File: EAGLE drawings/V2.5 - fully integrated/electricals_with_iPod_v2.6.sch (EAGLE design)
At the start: 47 parts, among them IC1 ATMEGA32U2-TQFP, Y1 16MHz

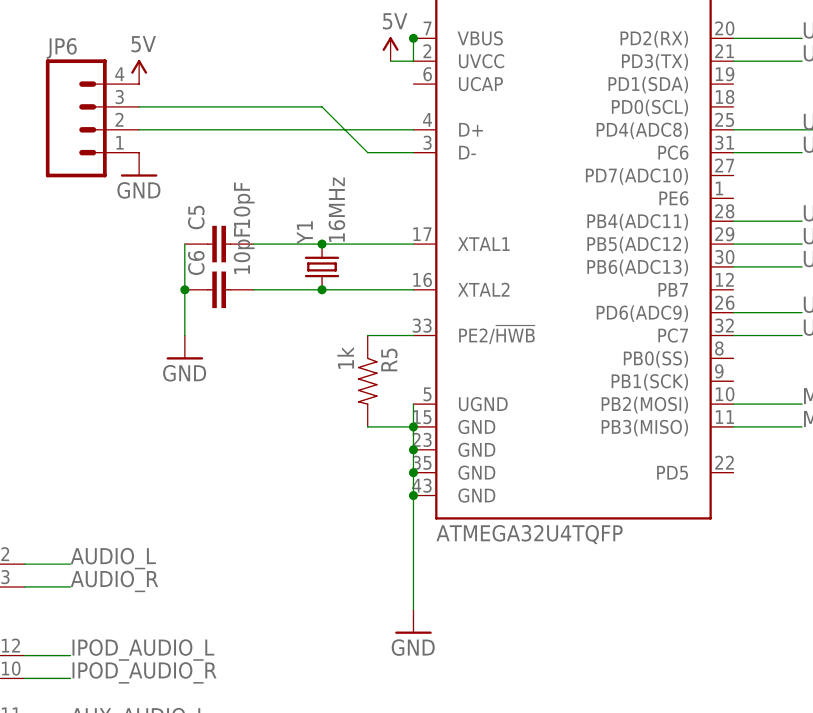
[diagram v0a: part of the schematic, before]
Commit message: Added v2.6 - smaller, 0603 passives, QFN mega*U4
Files edited with EAGLE 7.1.0
Split off v2.6
 - board about .25” shorter
 - 0603 passives
 - QFN package ATMega*U4
 - rearranged power supply
 - tweaked iPod connector board
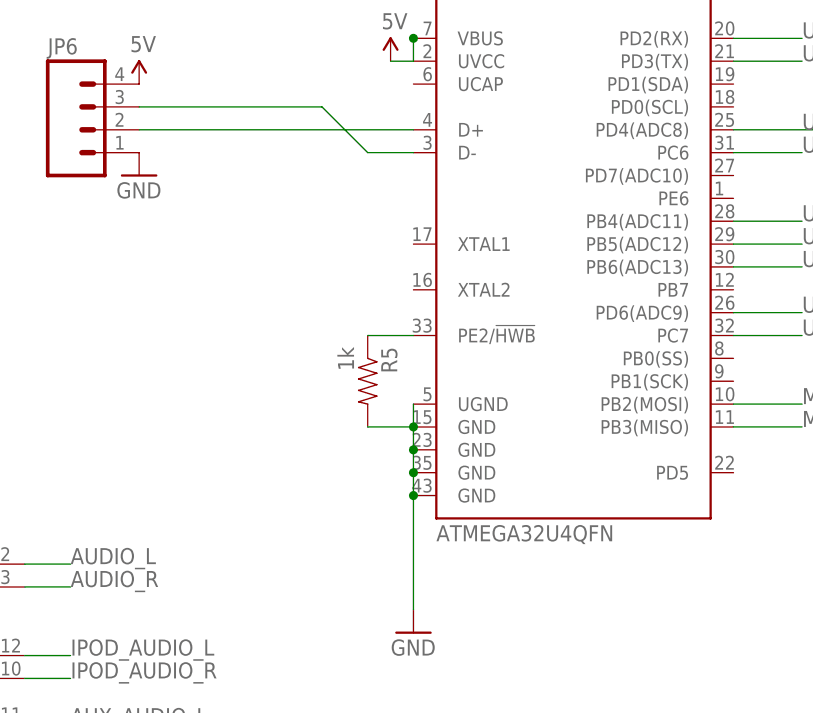
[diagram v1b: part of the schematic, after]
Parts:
- removed C5, C6: 10pF, SparkFun-Passives:CAP0805
- removed Y1: 16MHz, SparkFun-FreqCtrl:CRYSTAL5X3
- C1, C2, C3, C4, C7, C8, C9: device SparkFun-Passives:CAP0805 -> SparkFun-Passives:CAP0603-CAP
- R1, R2, R3, R4, R5, R6, R7: device SparkFun-Resistors:RESISTOR0805-RES -> SparkFun-Resistors:RESISTOR0603-RES
- U$8: value ATMEGA32U4TQFP -> ATMEGA32U4QFN; device SparkFun-DigitalIC:ATMEGA32U4TQFP -> SparkFun-DigitalIC:ATMEGA32U4QFN
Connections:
- removed net N$15: C5.2, U$8.XTAL1, Y1.2
- removed net N$28: C6.2, U$8.XTAL2, Y1.1
- net GND: no longer C5.1, C6.1

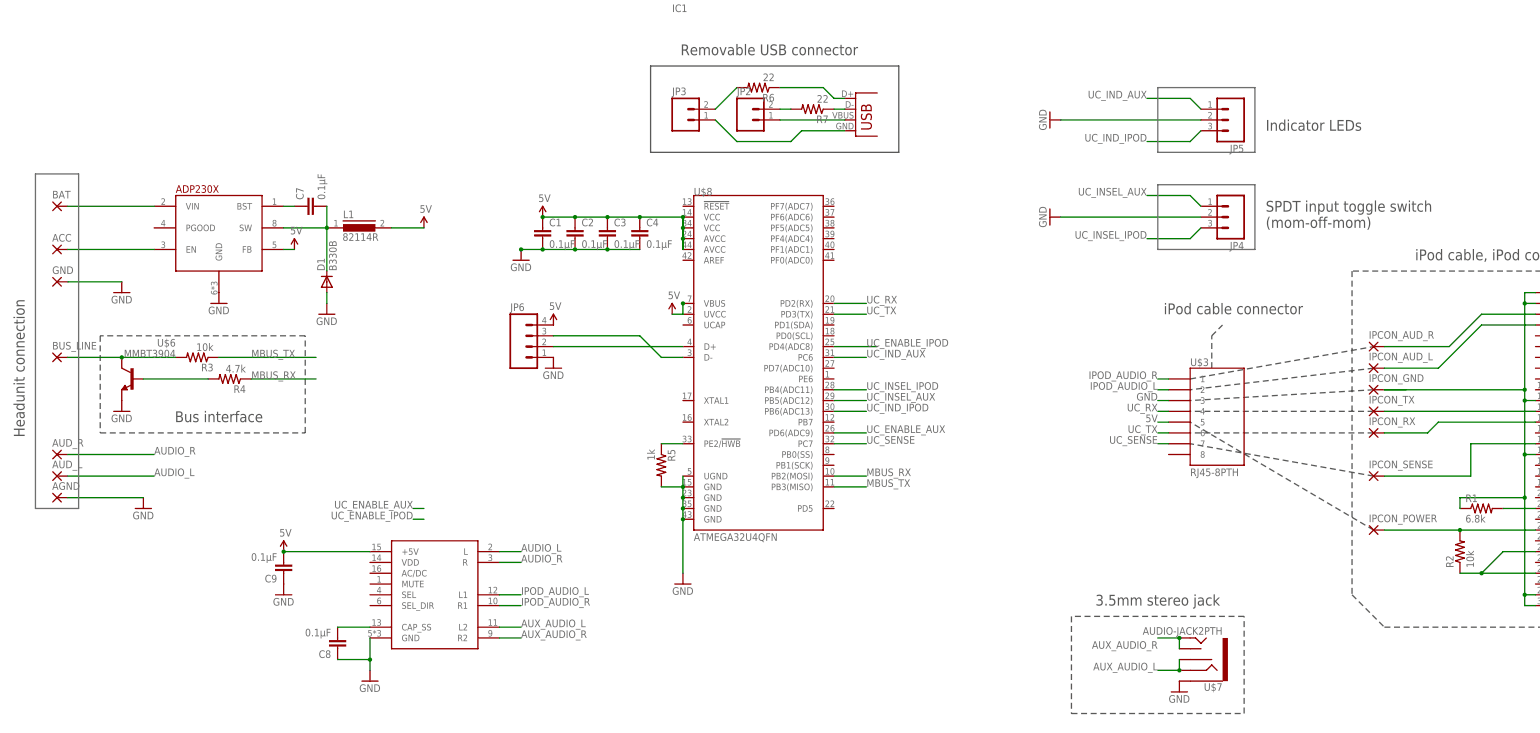
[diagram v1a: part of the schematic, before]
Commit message: iPod breakout split from v2.6, new single-input board
The iPod connector board was pulled from V2.6 to send to OSHPark

v2.6 is pending revisions down from the ATMega 16U4 to [8|16|32]U2. May
shrink more.

A new board is in the works that can fit on the back of the stereo
connector, providing only an auxiliary input. Uses an ATTiny.
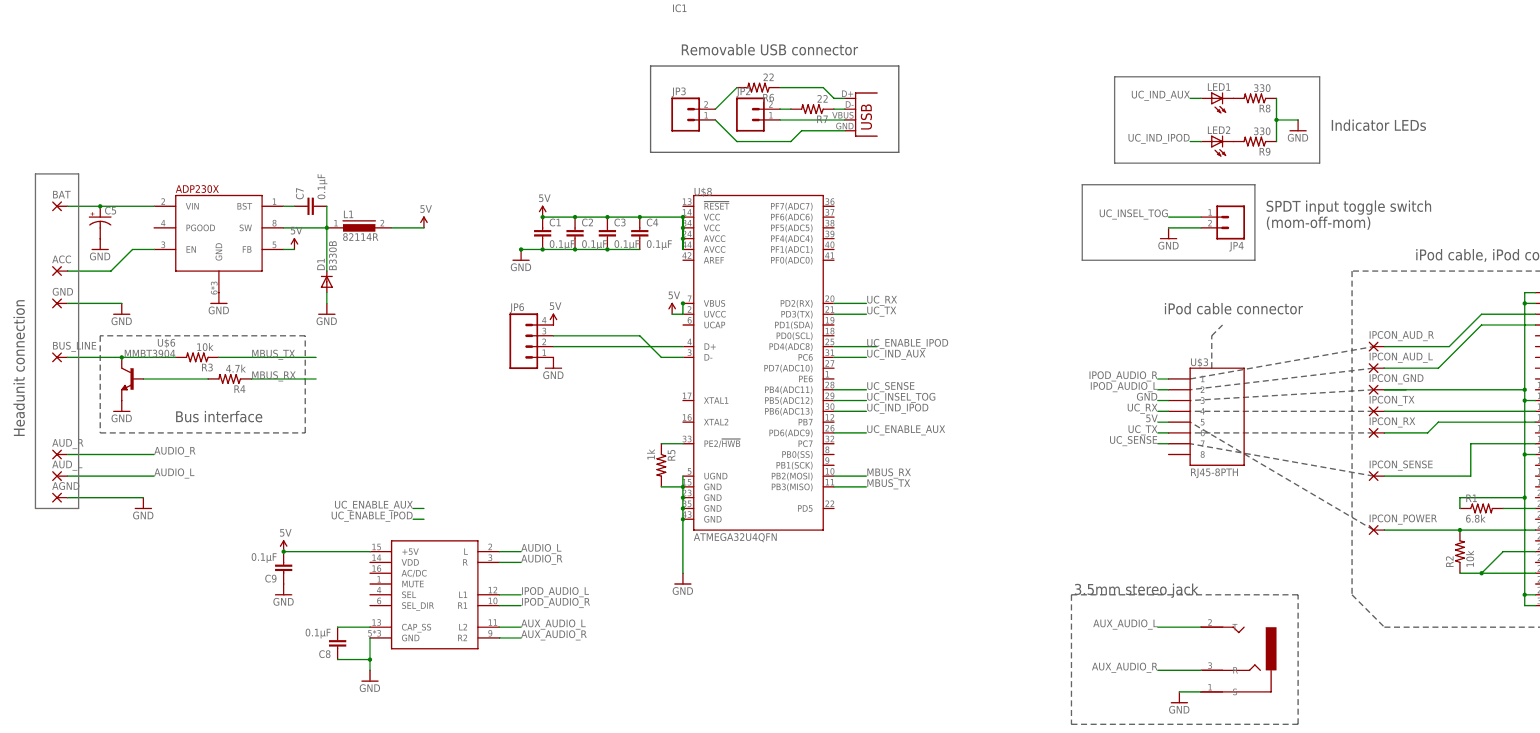
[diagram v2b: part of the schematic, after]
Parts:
- removed JP5: (no value), SparkFun-Connectors:M03LOCK
- added C5: (no value), SparkFun-Capacitors:CAP_POLPTH2
- added LED1, LED2: (no value), SparkFun-LED:LED0603
- added R8, R9: 330, SparkFun-Resistors:RESISTOR0603-RES
- JP4: device SparkFun-Connectors:M03LOCK -> SparkFun-Connectors:M02LOCK
- U$7: value AUDIO-JACK2PTH -> STEREO_JACK_SJ1-353XNG3NG; device SparkFun-Connectors:AUDIO-JACK2PTH -> personal:STEREO_JACK_SJ1-353XNG3NG
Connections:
- net UC_INSEL_AUX renamed UC_INSEL_TOG
- removed net UC_INSEL_IPOD: JP4.3, U$8.PB4(ADC11)
- new net N$15: LED1.C, R8.2
- new net N$16: LED2.C, R9.2
- net AUX_AUDIO_L: now also U$7.T; no longer U$7.RING, U$7.RSH
- net AUX_AUDIO_R: now also U$7.R; no longer U$7.TIP, U$7.TSH
- net GND: now also C5.-, R8.1, R9.1, U$7.S; no longer JP5.2, U$7.SLEEVE
- net N$2: now also C5.+
- net UC_IND_AUX: now also LED1.A; no longer JP5.1
- net UC_IND_IPOD: now also LED2.A; no longer JP5.3
- net UC_SENSE: now also U$8.PB4(ADC11); no longer U$8.PC7
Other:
- moved on the sheet: ACC, GND

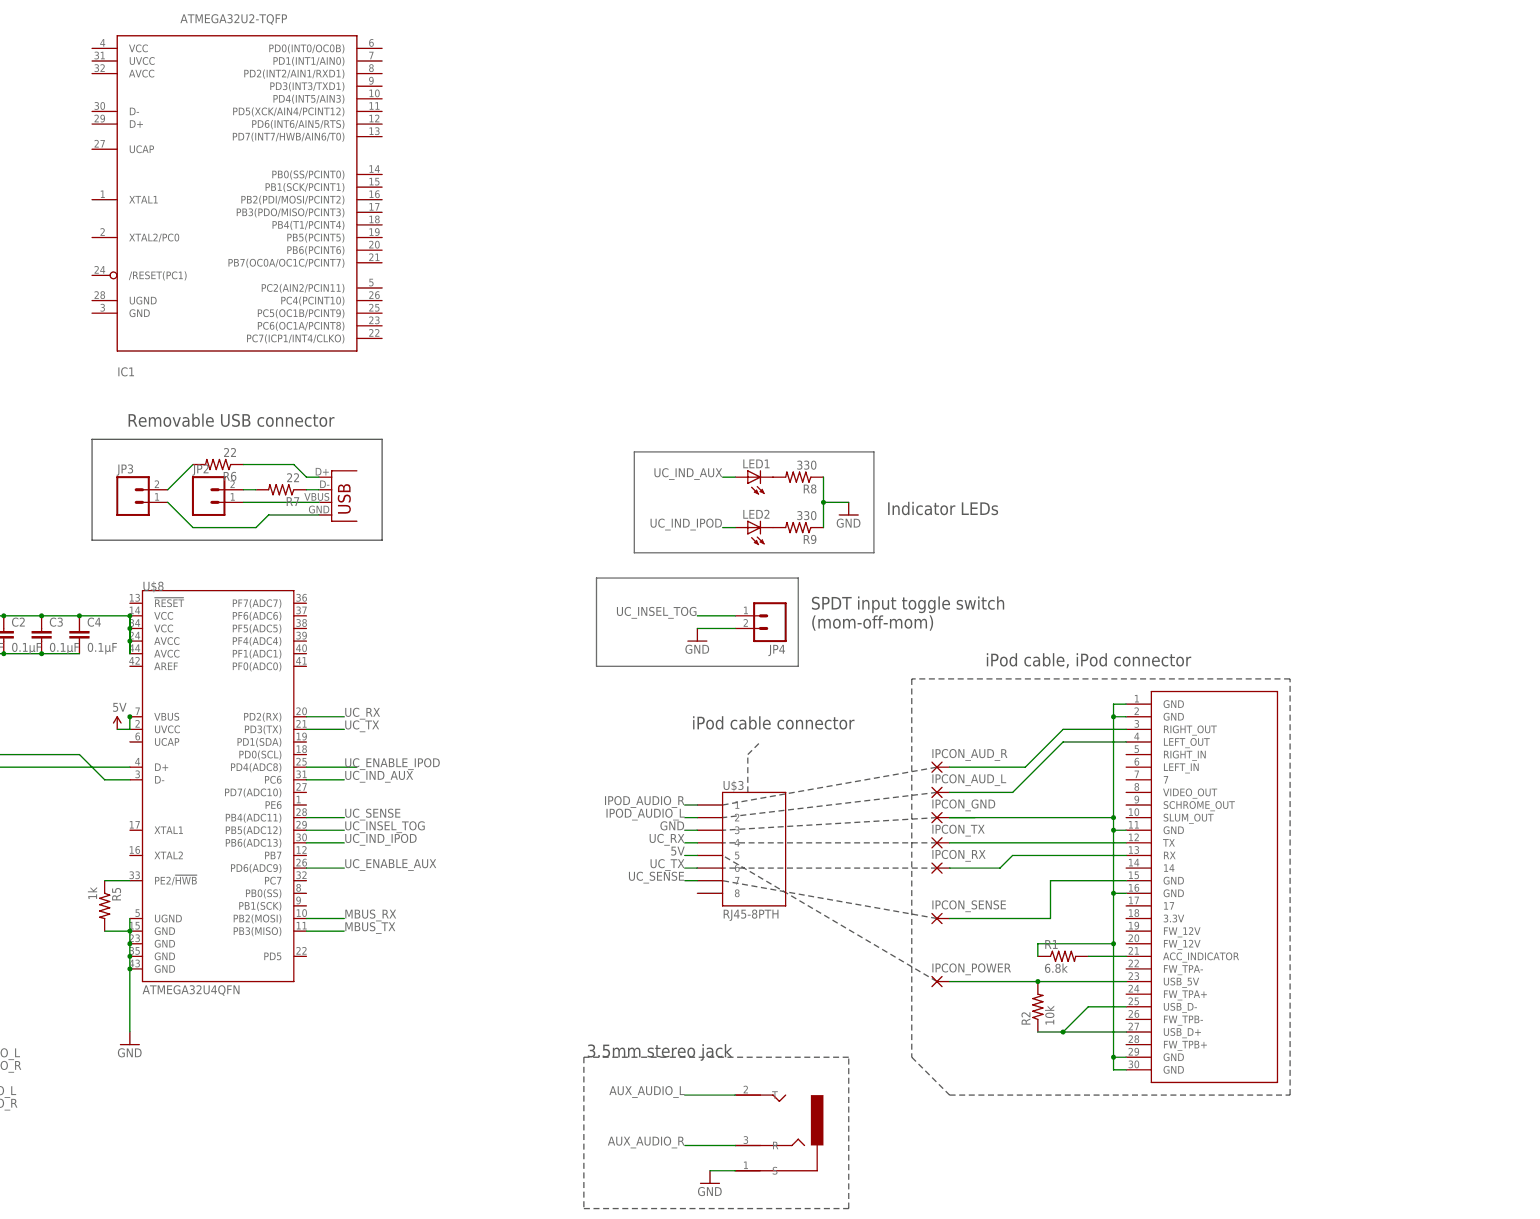
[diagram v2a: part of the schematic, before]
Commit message: Updated aux-only board, preparing to switch to 32/16/8U2
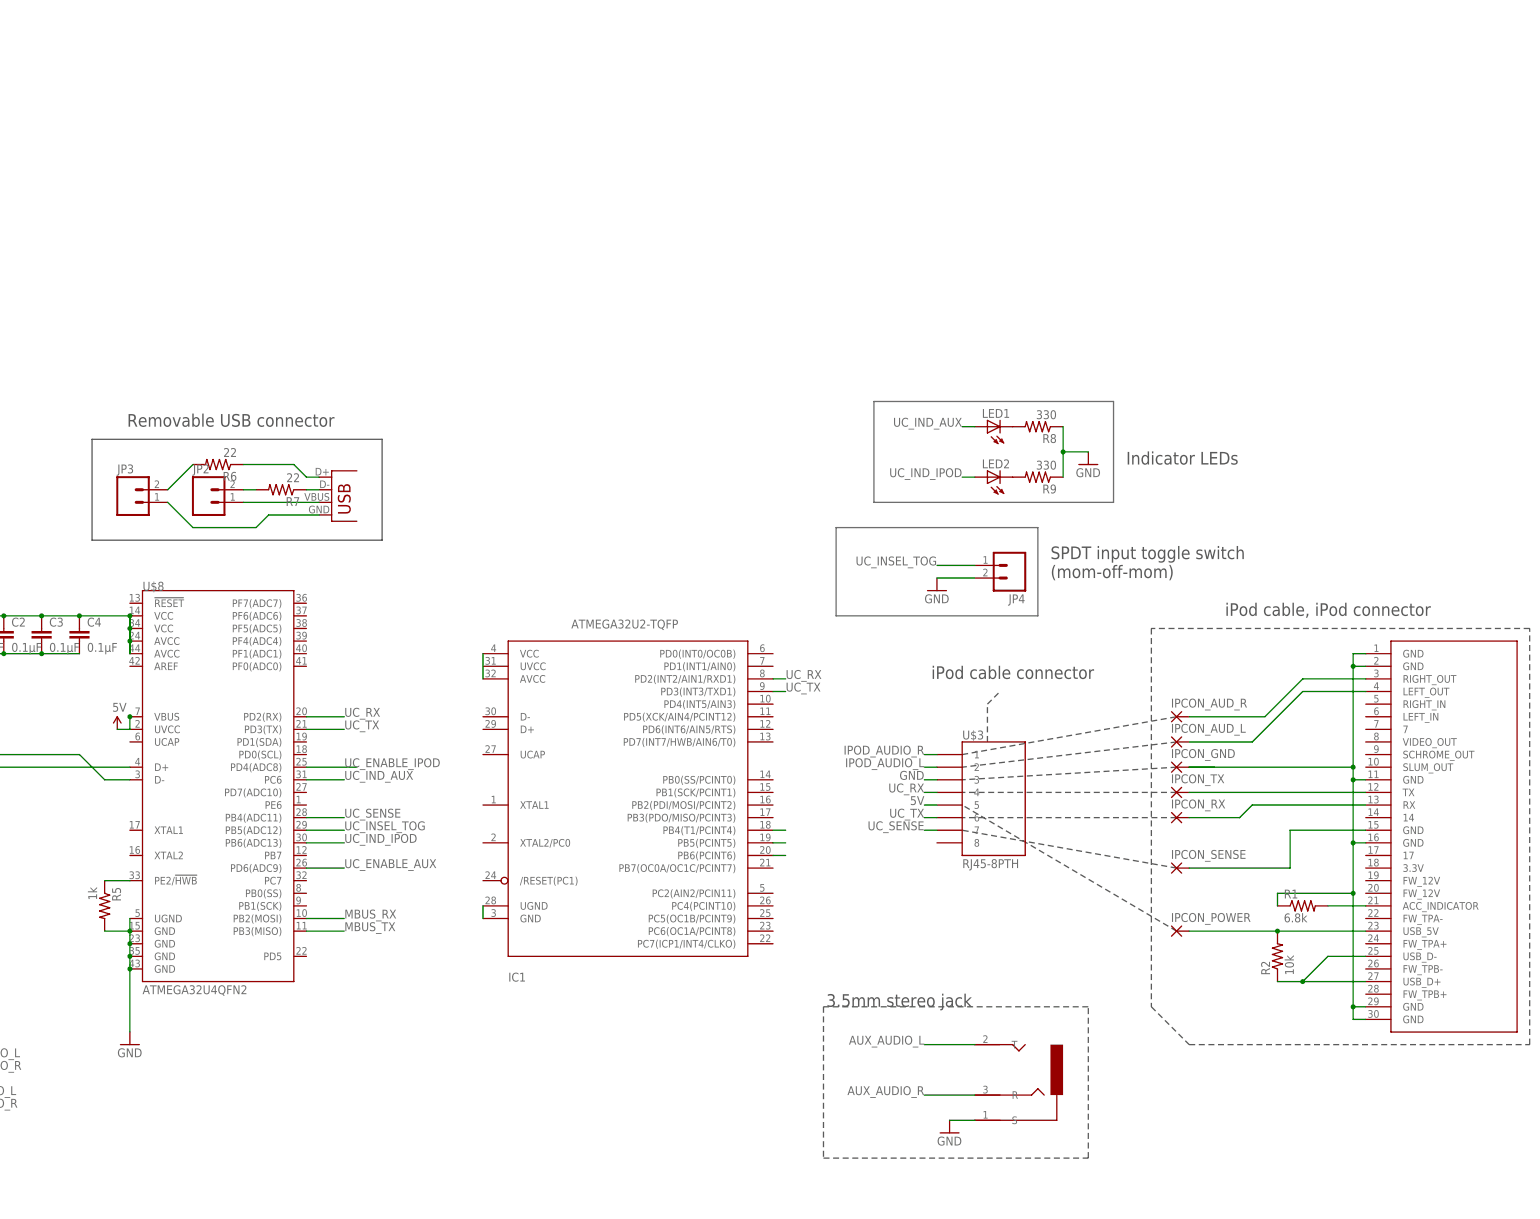
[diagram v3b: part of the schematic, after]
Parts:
- U$8: value ATMEGA32U4QFN -> ATMEGA32U4QFN2; device SparkFun-DigitalIC:ATMEGA32U4QFN -> SparkFun-DigitalIC:ATMEGA32U4QFN2
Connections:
- new net N$17: IC1.GND, IC1.UGND
- new net N$18: IC1.AVCC, IC1.VCC
- new net N$23: IC1.PB4(T1/PCINT4)
- new net N$24: IC1.PB5(PCINT5)
- new net N$25: IC1.PB6(PCINT6)
- net UC_RX: now also IC1.PD2(INT2/AIN1/RXD1)
- net UC_TX: now also IC1.PD3(INT3/TXD1)
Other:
- moved on the sheet: IC1, IPCON_AUD_L, IPCON_AUD_R, IPCON_GND, IPCON_POWER, IPCON_RX, IPCON_SENSE, IPCON_TX, JP4, LED1, LED2, R1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
